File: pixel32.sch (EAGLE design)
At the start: 83 parts, among them CON1 B7B-PH-K-S-SIDE, CON10 PINHEAD_1X01-2.54, CON11 PINHEAD_1X01-2.54, CON12 PINHEAD_1X02-2.54, CON13 PINHEAD_1X07-2, CON14 PINHEAD_1X07-2, CON2 B7B-PH-K-S-SIDE, CON3 PINHEAD_1X02-2.54, CON4 PINHEAD_1X01-2.54, CON5 PINHEAD_1X01-2.54, CON6 PINHEAD_1X01-2.54, CON7 PINHEAD_1X01-2.54, CON8 PINHEAD_1X01-2.54, CON9 PINHEAD_1X01-2.54, IC1 STM32F030K6TX-LQFP32(7X7), IC3 ST3485SOIC8, IC6 MC74VHC1GT125, IC7 MC74VHC1GT125, IC8 LM317, Y1 16MHz

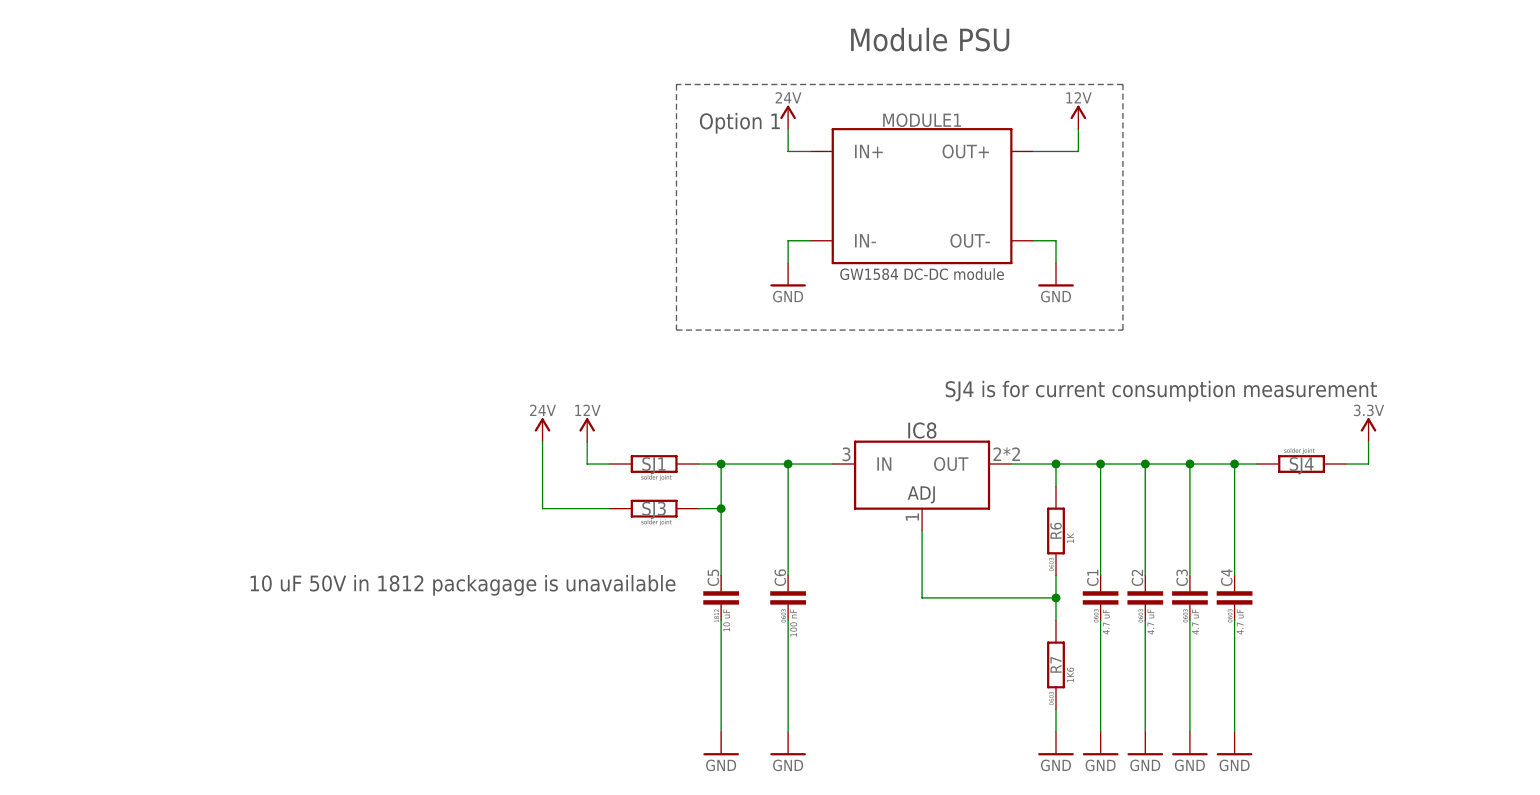
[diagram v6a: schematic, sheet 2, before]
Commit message: Added spare power connector just in case. New 3d view.
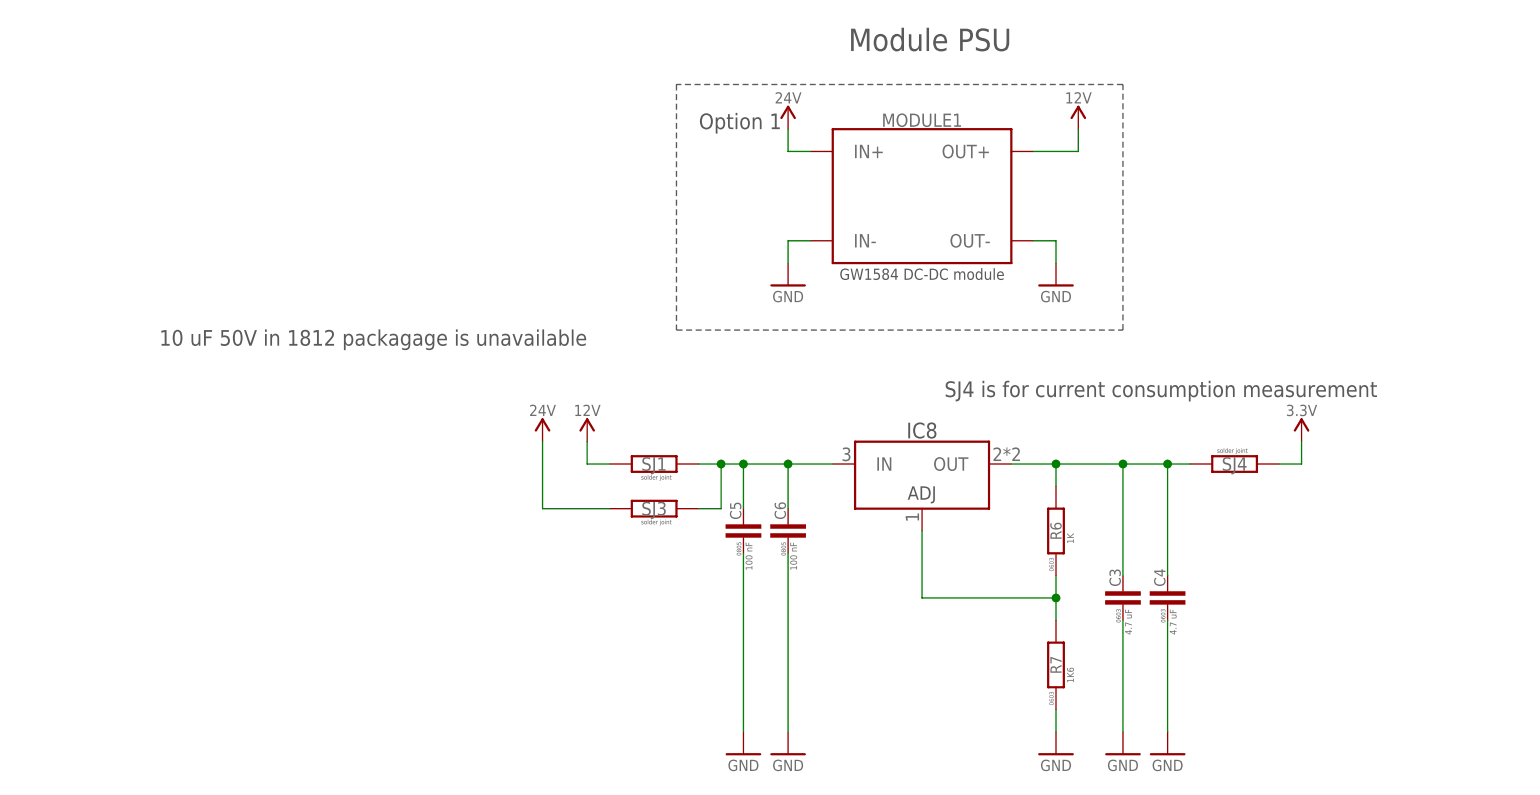
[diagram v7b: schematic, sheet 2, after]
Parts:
- removed C1, C2: 4.7 uF, rc:C-0603
- added CON15: (no value), led_matrix_master_lib:B2B-PH-K-S
- C5: value 10 uF -> 100 nF; device rc:C-1812 -> rc:C-0805; FARNELL# 2449143 -> 2496834; TME# CL32B106KBJNNNE -> GRM188R71H104KA93D
- C6: device rc:C-0603 -> rc:C-0805
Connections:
- removed net LED_CATHODE: C1.1
- net GND: now also CON15.+; no longer C1.1, C2.1
- net LED_ANODE: no longer C1.2
- net N$2: no longer C1.2, C2.2
- net SUPPLY: no longer C2.2
- net VDD_24V: now also CON15.-
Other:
- moved on the sheet: C3, C4, C5, C6, SJ4

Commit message: Moustashe added
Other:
- note added: "R1, R2 are for hardware version definition"
- note removed: "R1, R2 are for software version definition"
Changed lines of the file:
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@@
 <wire x1="259.08" y1="200.66" x2="200.66" y2="200.66" width="0.1524" layer="97" style="shortdash"/>
 <text x="203.2" y="203.2" size="2.54" layer="97">Maybe should get rid of it</text>
-<text x="114.3" y="175.26" size="1.778" layer="97">R1, R2 are for software version definition</text>
+<text x="114.3" y="175.26" size="1.778" layer="97">R1, R2 are for hardware version definition</text>
 <text x="114.3" y="172.72" size="1.778" layer="97">Do not mount</text>
 <text x="20.32" y="236.22" size="1.778" layer="97">Crystal load capacitance is 9 pF,
